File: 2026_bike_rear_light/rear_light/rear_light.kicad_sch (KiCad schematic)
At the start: 25 parts, among them J1 Conn_01x04, J2 Conn_01x05, Q1 2N5551, Q2 FQP27P06, Q3 2N5551, Q4 FQP27P06, Q5 2N5551, Q6 2N5551, Q7 FQP27P06, U1 LM2596HV

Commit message: Bike Rear Light - pcb layout, this time with modules and for hand soldering
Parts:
- removed ATtiny85: Conn_01x06, Connector_PinHeader_1.00mm:PinHeader_1x06_P1.00mm_Vertical, symbol Connector_Generic:Conn_01x06
- removed ATtiny85_pwr1: Conn_01x03, Connector_PinHeader_1.00mm:PinHeader_1x03_P1.00mm_Vertical, symbol Connector_Generic:Conn_01x03
- removed U1: LM2596HV, Package_TO_SOT_SMD:TO-263-5_TabPin3, symbol Regulator_Switching:GL2576-5.0TA5R
- added ATtiny85: Conn_01x09, models:Digispark, symbol Connector_Generic:Conn_01x09
- added U1: YAAJ_DCDC_StepDown_LM2596, models:YAAJ_DCDC_StepDown_LM2596, symbol yaaj_dcdc_stepdown_lm2596:YAAJ_DCDC_StepDown_LM2596
- R1, R10, R2, R4, R6: footprint Resistor_THT:R_Axial_DIN0204_L3.6mm_D1.6mm_P1.90mm_Vertical -> Resistor_THT:R_Axial_DIN0207_L6.3mm_D2.5mm_P5.08mm_Vertical
- R11, R3, R5, R7, R8, R9: footprint Resistor_THT:R_Axial_DIN0204_L3.6mm_D1.6mm_P1.90mm_Vertical -> Resistor_THT:R_Axial_DIN0207_L6.3mm_D2.5mm_P7.62mm_Horizontal
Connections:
- net BRAKE_LIGHT: now also ATtiny85.3 (Pin_3)
- net GND: now also ATtiny85.8 (Pin_8), U1.2 (GND), U1.3 (GND)
- net PB0: now also ATtiny85.1 (Pin_1)
- net PB1: now also ATtiny85.2 (Pin_2)
- net PB3: now also ATtiny85.4 (Pin_4)
- net PB4: now also ATtiny85.5 (Pin_5)
- net PB5: now also ATtiny85.6 (Pin_6)
- net VCC: now also ATtiny85.9 (Pin_9)
- net VIN: now also ATtiny85.7 (Pin_7), U1.4 (Vout)
- net at Q4.2 (D): now also U1.1 (Vin)
- no-connect marks 4 -> 1
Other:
- note added: "ATtiny85 Dev Board USB-A male"

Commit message: Bike Rear Light - Update ATTiny85 pin wiring
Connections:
- net PB0: now also R11.1
- net PB3: no longer R11.1
- net PB4: now also R9.1
- net PB5: no longer R9.1
- no-connect marks 1 -> 3
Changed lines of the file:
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@@
 		(at 153.67 49.53)
 	)
+	(no_connect
+		(at 58.42 44.45)
+	)
+	(no_connect
+		(at 58.42 49.53)
+	)
 	(wire
 		(pts
@@
 	(wire
 		(pts
-			(xy 58.42 44.45) (xy 63.5 44.45)
-		)
-		(stroke
-			(width 0)
-			(type default)
-		)
-	)
-	(wire
-		(pts
 			(xy 27.94 134.62) (xy 33.02 134.62)
 		)
@@
 	(wire
 		(pts
-			(xy 33.02 143.51) (xy 33.02 146.05)
+			(xy 27.94 114.3) (xy 27.94 111.76)
+		)
+		(stroke
+			(width 0)
+			(type default)
+		)
+	)
+	(wire
+		(pts
+			(xy 33.02 143.51) (xy 33.02 149.86)
 		)
 		(stroke
@@
 	(wire
 		(pts
-			(xy 27.94 146.05) (xy 33.02 146.05)
+			(xy 34.29 149.86) (xy 33.02 149.86)
 		)
 		(stroke
@@
 	(wire
 		(pts
+			(xy 58.42 46.99) (xy 63.5 46.99)
+		)
+		(stroke
+			(width 0)
+			(type default)
+		)
+	)
+	(wire
+		(pts
+			(xy 58.42 57.15) (xy 63.5 57.15)
+		)
+		(stroke
+			(width 0)
+			(type default)
+		)
+	)
+	(wire
+		(pts
 			(xy 212.09 118.11) (xy 212.09 116.84)
 		)
@@
 	(wire
 		(pts
+			(xy 58.42 54.61) (xy 63.5 54.61)
+		)
+		(stroke
+			(width 0)
+			(type default)
+		)
+	)
+	(wire
+		(pts
 			(xy 58.42 35.56) (xy 58.42 36.83)
 		)
@@
 	(wire
 		(pts
-			(xy 63.5 49.53) (xy 58.42 49.53)
-		)
-		(stroke
-			(width 0)
-			(type default)
-		)
-	)
-	(wire
-		(pts
 			(xy 238.76 129.54) (xy 238.76 133.35)
 		)
@@
 			(width 0)
 			(type default)
+		)
+	)
+	(label "LEFT"
+		(at 236.22 53.34 180)
+		(effects
+			(font
+				(size 1.27 1.27)
+			)
+			(justify right bottom)
+		)
+	)
+	(label "BATT"
+		(at 73.66 109.22 0)
+		(effects
+			(font
+				(size 1.27 1.27)
+			)
+			(justify left bottom)
+		)
+	)
+	(label "PB2"
+		(at 58.42 52.07 0)
+		(effects
+			(font
+				(size 1.27 1.27)
+			)
+			(justify left bottom)
+		)
+	)
+	(label "BATT"
+		(at 156.21 46.99 0)
+		(effects
+			(font
+				(size 1.27 1.27)
+			)
+			(justify left bottom)
+		)
+	)
+	(label "PB1"
+		(at 58.42 54.61 0)
+		(effects
+			(font
+				(size 1.27 1.27)
+			)
+			(justify left bottom)
+		)
+	)
+	(label "PWR_CONTROL"
+		(at 63.5 46.99 0)
+		(effects
+			(font
+				(size 1.27 1.27)
+			)
+			(justify left bottom)
+		)
+	)
+	(label "BATT"
+		(at 166.37 110.49 0)
+		(effects
+			(font
+				(size 1.27 1.27)
+			)
+			(justify left bottom)
+		)
+	)
+	(label "PB4"
+		(at 58.42 46.99 0)
+		(effects
+			(font
+				(size 1.27 1.27)
+			)
+			(justify left bottom)
+		)
+	)
+	(label "BRAKE"
+		(at 236.22 55.88 180)
+		(effects
+			(font
+				(size 1.27 1.27)
+			)
+			(justify right bottom)
+		)
+	)
+	(label "SYS"
+		(at 151.13 45.72 0)
+		(effects
+			(font
+				(size 1.27 1.27)
+			)
+			(justify left bottom)
+		)
+	)
+	(label "SYS_PWR_READ"
+		(at 63.5 57.15 0)
+		(effects
+			(font
+				(size 1.27 1.27)
+			)
+			(justify left bottom)
+		)
+	)
+	(label "SYS"
+		(at 27.94 134.62 0)
+		(effects
+			(font
+				(size 1.27 1.27)
+			)
+			(justify left bottom)
+		)
+	)
+	(label "PB5"
+		(at 58.42 44.45 0)
+		(effects
+			(font
+				(size 1.27 1.27)
+			)
+			(justify left bottom)
+		)
+	)
+	(label "TAIL"
+		(at 168.91 130.81 0)
+		(effects
+			(font
+				(size 1.27 1.27)
+			)
+			(justify left bottom)
 		)
 	)
@@
 		)
 	)
+	(label "SYS_PWR_READ"
+		(at 34.29 149.86 0)
+		(effects
+			(font
+				(size 1.27 1.27)
+			)
+			(justify left bottom)
+		)
+	)
 	(label "TAIL_LIGHT"
 		(at 63.5 54.61 0)
@@
 		)
 	)
-	(label "LEFT"
-		(at 236.22 53.34 180)
-		(effects
-			(font
-				(size 1.27 1.27)
-			)
-			(justify right bottom)
-		)
-	)
-	(label "BATT"
-		(at 73.66 109.22 0)
-		(effects
-			(font
-				(size 1.27 1.27)
-			)
-			(justify left bottom)
-		)
-	)
-	(label "PB2"
-		(at 58.42 52.07 0)
-		(effects
-			(font
-				(size 1.27 1.27)
-			)
-			(justify left bottom)
-		)
-	)
-	(label "BATT"
-		(at 156.21 46.99 0)
-		(effects
-			(font
-				(size 1.27 1.27)
-			)
-			(justify left bottom)
-		)
-	)
-	(label "SYS_PWR_READ"
-		(at 63.5 49.53 0)
-		(effects
-			(font
-				(size 1.27 1.27)
-			)
-			(justify left bottom)
-		)
-	)
-	(label "PB1"
-		(at 58.42 54.61 0)
-		(effects
-			(font
-				(size 1.27 1.27)
-			)
-			(justify left bottom)
-		)
-	)
-	(label "BATT"
-		(at 166.37 110.49 0)
-		(effects
-			(font
-				(size 1.27 1.27)
-			)
-			(justify left bottom)
-		)
-	)
-	(label "PB4"
-		(at 58.42 46.99 0)
-		(effects
-			(font
-				(size 1.27 1.27)
-			)
-			(justify left bottom)
-		)
-	)
-	(label "BRAKE"
-		(at 236.22 55.88 180)
-		(effects
-			(font
-				(size 1.27 1.27)
-			)
-			(justify right bottom)
-		)
-	)
-	(label "SYS"
-		(at 151.13 45.72 0)
-		(effects
-			(font
-				(size 1.27 1.27)
-			)
-			(justify left bottom)
-		)
-	)
-	(label "SYS"
-		(at 27.94 134.62 0)
-		(effects
-			(font
-				(size 1.27 1.27)
-			)
-			(justify left bottom)
-		)
-	)
-	(label "PB5"
-		(at 58.42 44.45 0)
-		(effects
-			(font
-				(size 1.27 1.27)
-			)
-			(justify left bottom)
-		)
-	)
-	(label "TAIL"
-		(at 168.91 130.81 0)
-		(effects
-			(font
-				(size 1.27 1.27)
-			)
-			(justify left bottom)
-		)
-	)
-	(label "PB3"
-		(at 27.94 146.05 0)
-		(effects
-			(font
-				(size 1.27 1.27)
-			)
-			(justify left bottom)
-		)
-	)
-	(label "PB2"
+	(label "BRAKE_LIGHT"
 		(at 207.01 116.84 0)
-		(effects
-			(font
-				(size 1.27 1.27)
-			)
-			(justify left bottom)
-		)
-	)
-	(label "PB5"
-		(at 27.94 114.3 0)
 		(effects
 			(font
@@
 	)
 	(label "PWR_CONTROL"
-		(at 63.5 44.45 0)
+		(at 27.94 111.76 0)
 		(effects
 			(font
@@
 		)
 	)
-	(label "PB1"
+	(label "TAIL_LIGHT"
 		(at 134.62 114.3 0)
 		(effects
@@
 		(on_board yes)
 		(dnp no)
-		(fields_autoplaced yes)
 		(property "Reference" "R9"
-			(at 36.83 107.95 90)
+			(at 36.83 116.84 90)
 			(effects
 				(font
@@
 		)
 		(property "Value" "10k"
-			(at 36.83 110.49 90)
-			(effects
-				(font
+			(at 36.83 119.38 90)
+			(effects
+				(font

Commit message: Bike Rear Light - Update PCB for molex connectors
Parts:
- J1: footprint Connector_PinHeader_1.00mm:PinHeader_1x04_P1.00mm_Vertical -> Connector_Molex:Molex_KK-254_AE-6410-04A_1x04_P2.54mm_Vertical
- J2: footprint Connector_PinHeader_1.00mm:PinHeader_1x05_P1.00mm_Vertical_SMD_Pin1Left -> Connector_Molex:Molex_KK-254_AE-6410-05A_1x05_P2.54mm_Vertical
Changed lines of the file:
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@@
 			)
 		)
-		(property "Footprint" "Connector_PinHeader_1.00mm:PinHeader_1x04_P1.00mm_Vertical"
+		(property "Footprint" "Connector_Molex:Molex_KK-254_AE-6410-04A_1x04_P2.54mm_Vertical"
 			(at 153.67 54.61 0)
 			(effects
@@
 			)
 		)
-		(property "Footprint" "Connector_PinHeader_1.00mm:PinHeader_1x05_P1.00mm_Vertical_SMD_Pin1Left"
+		(property "Footprint" "Connector_Molex:Molex_KK-254_AE-6410-05A_1x05_P2.54mm_Vertical"
 			(at 224.79 53.34 0)
 			(effects

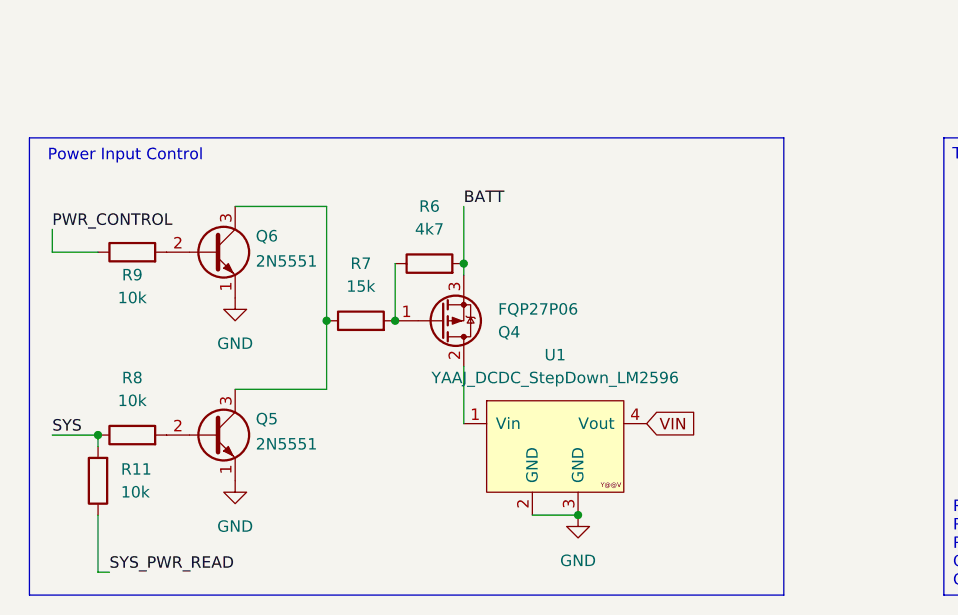
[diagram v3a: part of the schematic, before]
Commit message: Bike Rear Light - Update Schematic and PCB (remove MOSFET)
 - Alter circuit so that it controls the buck converter via its enablement pin
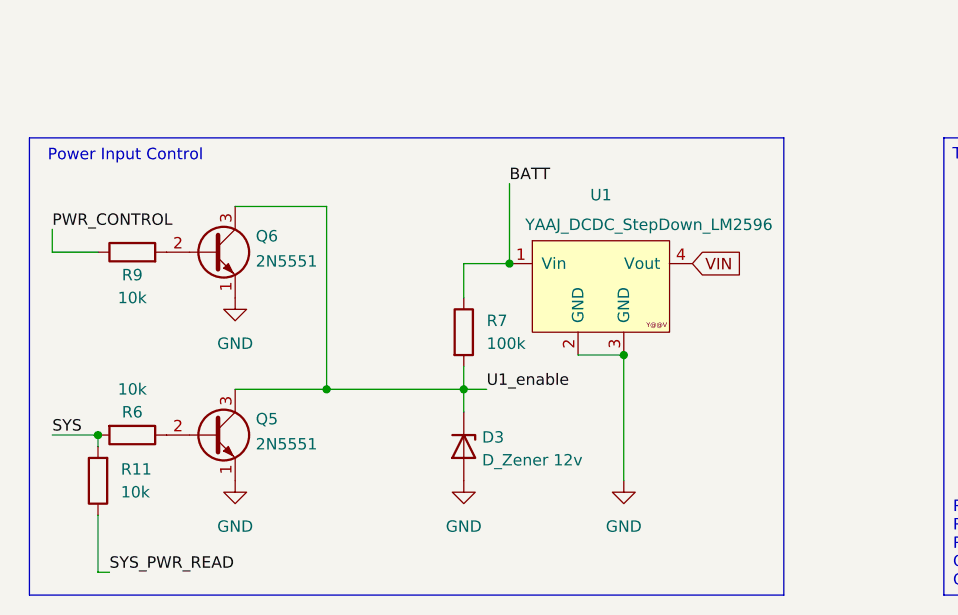
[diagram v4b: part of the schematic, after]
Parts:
- removed Q4: FQP27P06, Package_TO_SOT_THT:TO-220-3_Vertical, symbol Transistor_FET:FQP27P06
- removed R8: 10k, Resistor_THT:R_Axial_DIN0207_L6.3mm_D2.5mm_P7.62mm_Horizontal, symbol Device:R
- added D3: D_Zener 12v, Diode_THT:D_DO-41_SOD81_P10.16mm_Horizontal, symbol Device:D_Zener
- R6: value 4k7 -> 10k; footprint Resistor_THT:R_Axial_DIN0207_L6.3mm_D2.5mm_P5.08mm_Vertical -> Resistor_THT:R_Axial_DIN0207_L6.3mm_D2.5mm_P7.62mm_Horizontal
- R7: value 15k -> 100k
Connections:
- net +48V: now also R7.1, U1.1 (Vin); no longer R6.2
- net +5V: now also R6.2
- net GND: now also D3.2 (A)
- net U1_enable: now reaches Q5.3 (C), Q6.3 (C)
- net U1_enable: now also R7.2, D3.1 (K); no longer R7.1
- net at R6.1: now also Q5.2 (B); no longer R7.2
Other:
- moved on the sheet: U1

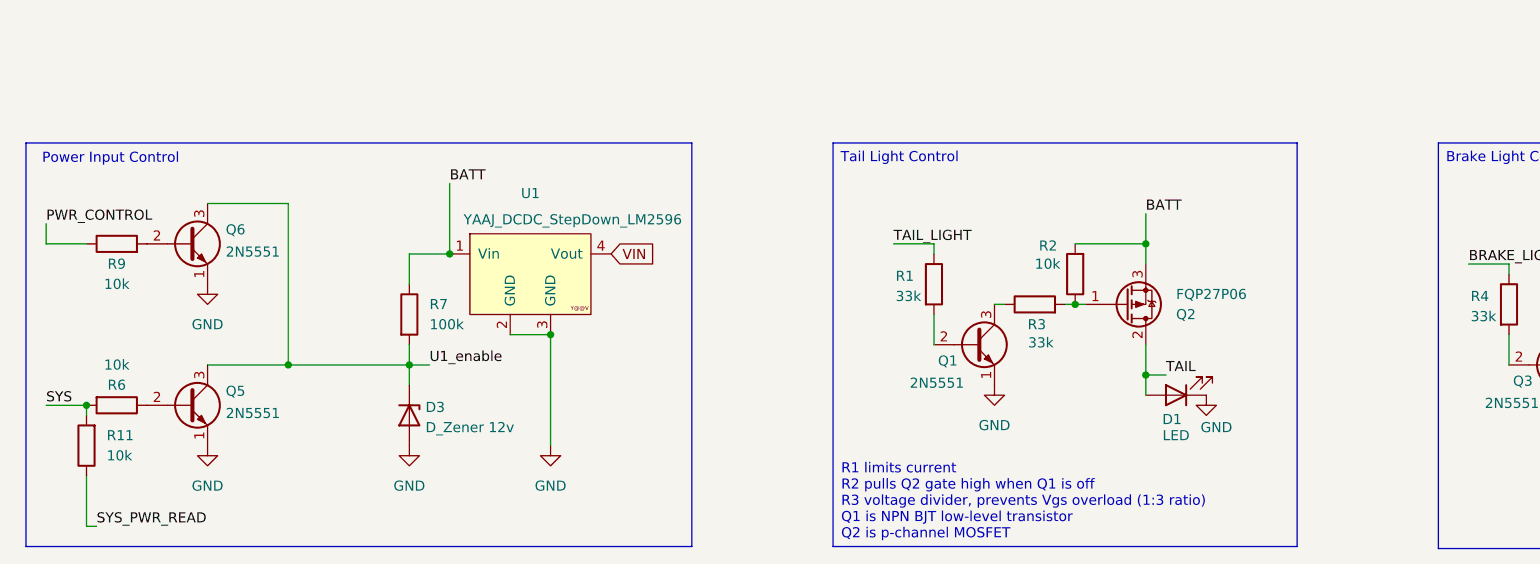
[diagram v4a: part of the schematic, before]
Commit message: Bike Rear Light - Update circuit for new buck converter
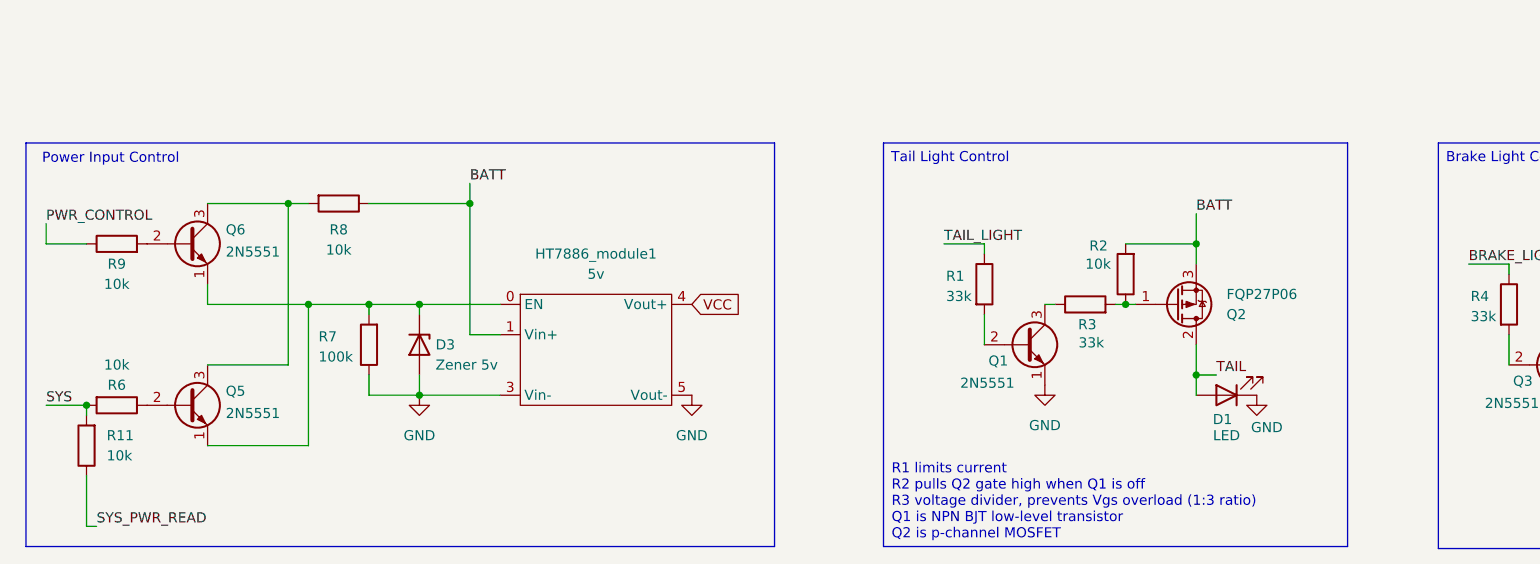
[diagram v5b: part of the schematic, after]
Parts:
- removed U1: YAAJ_DCDC_StepDown_LM2596, models:YAAJ_DCDC_StepDown_LM2596, symbol yaaj_dcdc_stepdown_lm2596:YAAJ_DCDC_StepDown_LM2596
- added HT7886_module1: 5v, HT7886:DC-DC_100V_3.5A_step_down, symbol HT7886:Module
- added R8: 10k, Resistor_THT:R_Axial_DIN0207_L6.3mm_D2.5mm_P7.62mm_Horizontal, symbol Device:R
- D3: value D_Zener 12v -> Zener 5v
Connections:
- net +48V: now also HT7886_module1.1 (Vin+), R8.1; no longer R7.1
- net GND: now also R7.1, HT7886_module1.3 (Vin-), HT7886_module1.5 (Vout-); no longer Q5.1 (E), Q6.1 (E)
- net VCC: now also HT7886_module1.4 (Vout+)
- net U1_enable: no longer names the net of D3.1 (K), R7.2
- net U1_enable: now also Q5.1 (E), Q6.1 (E), HT7886_module1.0 (EN); no longer Q5.3 (C), Q6.3 (C)
- new net: Q5.3 (C), Q6.3 (C), R8.2
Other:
- moved on the sheet: D1, D3, Q1, Q2, R1, R2, R3, R7
